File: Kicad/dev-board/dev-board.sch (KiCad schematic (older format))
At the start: 50 parts

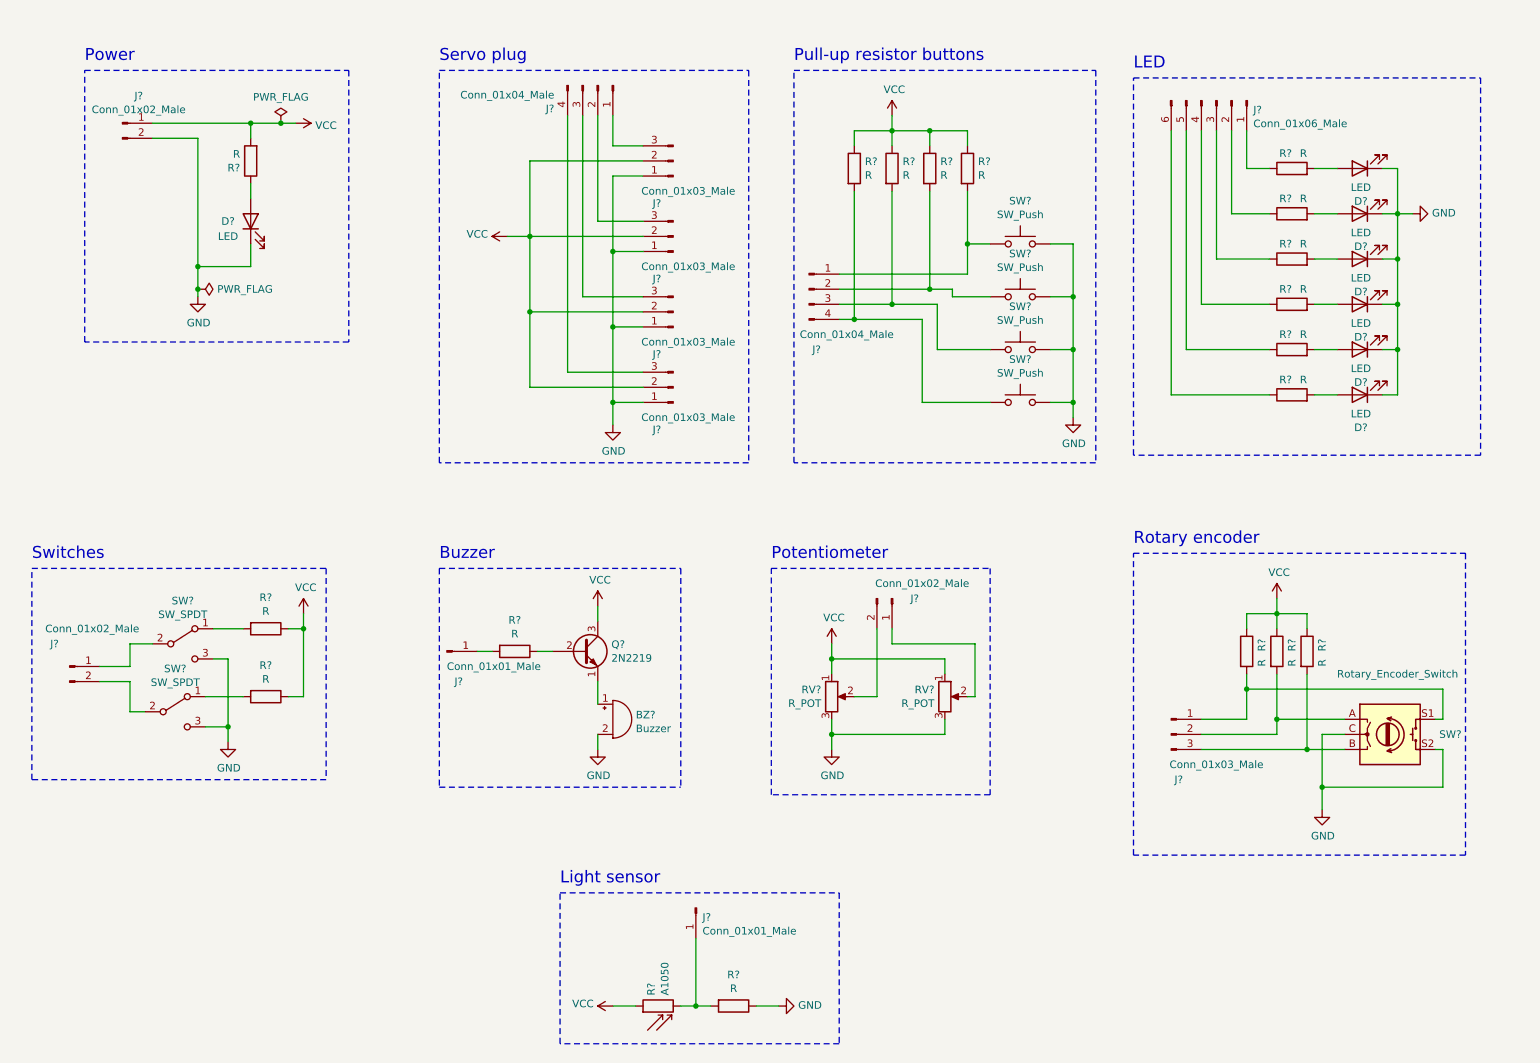
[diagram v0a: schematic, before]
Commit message: Add 555 timer + DIP switches
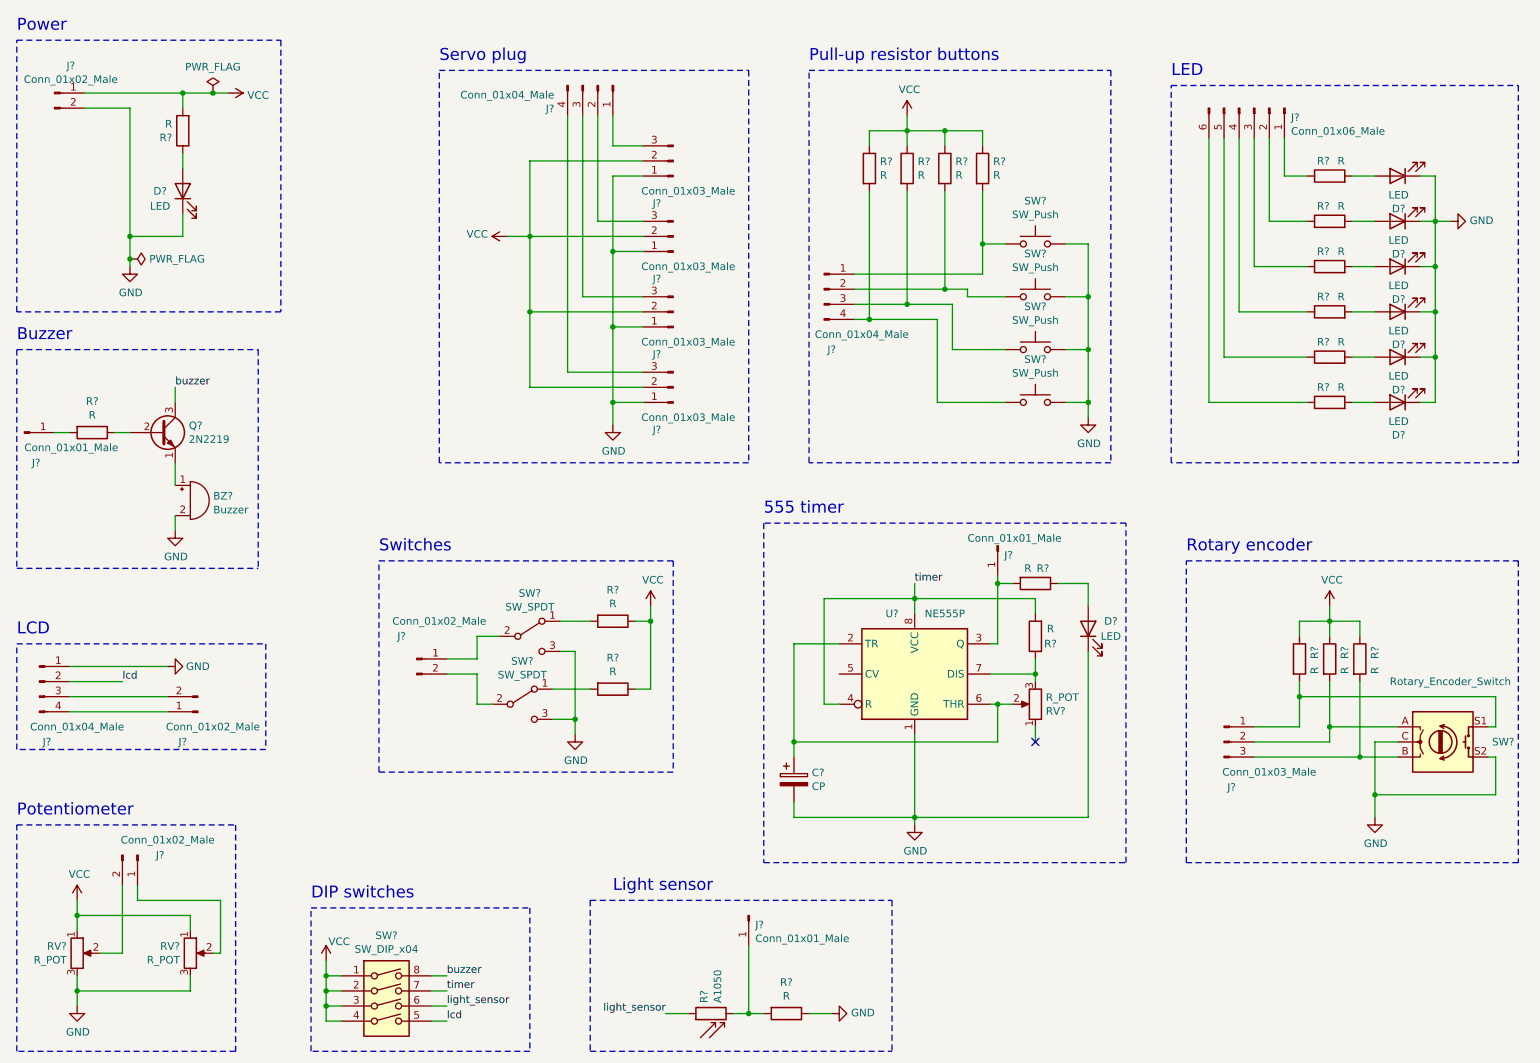
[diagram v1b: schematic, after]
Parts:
- added C?: CP, symbol Device:CP
- added D?: LED, symbol Device:LED
- added J?: Conn_01x01_Male, symbol Connector:Conn_01x01_Male
- added J?: Conn_01x04_Male, symbol Connector:Conn_01x04_Male
- added J?: Conn_01x02_Male, symbol Connector:Conn_01x02_Male
- added R? (x2): R, symbol Device:R
- added RV?: R_POT, symbol Device:R_POT
- added SW?: SW_DIP_x04, symbol Switch:SW_DIP_x04
- added U?: NE555P, Package_DIP:DIP-8_W7.62mm, symbol Timer:NE555P
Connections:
- net GND: now also C?.2, D?.1 (K), J?.1 (Pin_1), U?.1 (GND)
- net VCC: now also SW?.1, SW?.2, SW?.3, SW?.4; no longer Q?.3 (C), R?.1
- new net: C?.1, RV?.2, U?.2 (TR), U?.6 (THR)
- new net: J?.1 (Pin_1), R?.2, U?.3 (Q)
- new net: R?.1, RV?.3, U?.7 (DIS)
- new net: D?.2 (A), R?.1
- new net: J?.2 (Pin_2), J?.3 (Pin_3)
- new net: J?.1 (Pin_1), J?.4 (Pin_4)
- new net buzzer: Q?.3 (C), SW?.8
- new net lcd: J?.2 (Pin_2), SW?.5
- new net light_sensor: R?.1, SW?.6
- new net timer: R?.2, SW?.7, U?.4 (R), U?.8 (VCC)
- no-connect marks 0 -> 1
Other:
- note added: "555 timer"
- note added: "DIP switches"
- note added: "LCD"
- moved on the sheet: BZ?, D?, J?, Q?, R?, RV?, SW?

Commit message: Assign Footprint
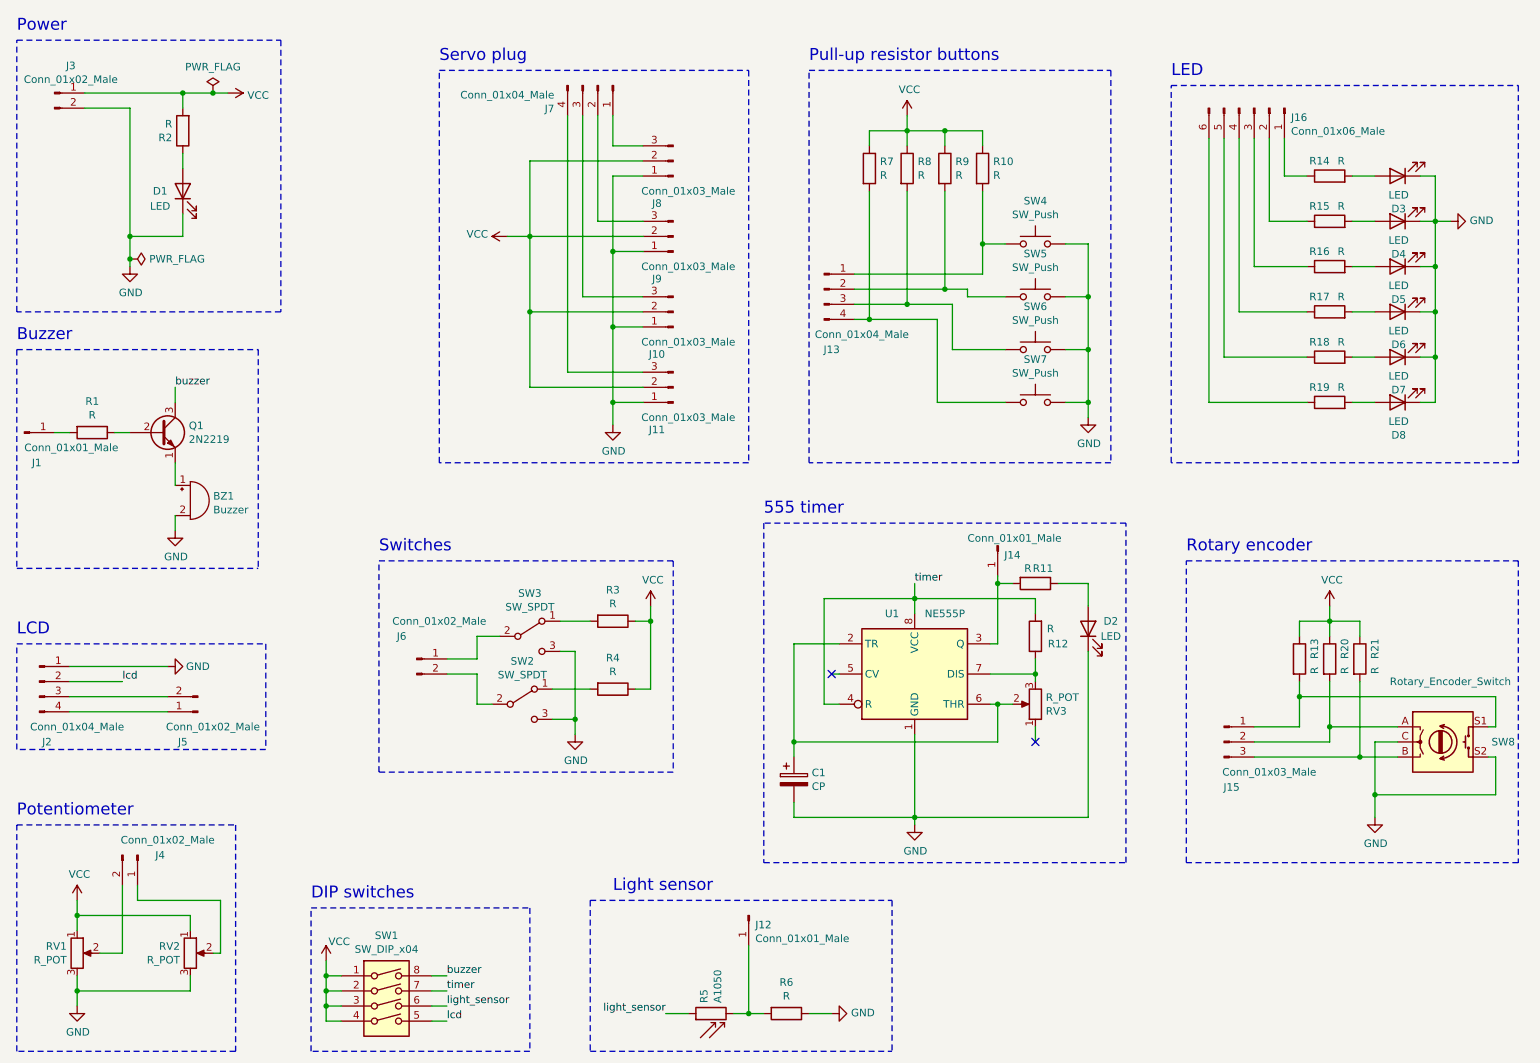
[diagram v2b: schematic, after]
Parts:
- BZ1: renamed from BZ?; footprint (none) -> Buzzer_Beeper:Buzzer_12x9.5RM7.6
- C1: renamed from C?; footprint (none) -> Capacitor_SMD:CP_Elec_5x5.3
- D1, D2, D3, D4, D5, D6, D7, D8: renamed from D?; footprint (none) -> LED_SMD:LED_0805_2012Metric_Pad1.15x1.40mm_HandSolder
- J1, J12, J14: renamed from J?; footprint (none) -> Connector_PinHeader_2.54mm:PinHeader_1x01_P2.54mm_Vertical
- J10, J11, J15, J8, J9: renamed from J?; footprint (none) -> Connector_PinHeader_2.54mm:PinHeader_1x03_P2.54mm_Vertical
- J13, J2, J7: renamed from J?; footprint (none) -> Connector_PinHeader_2.54mm:PinHeader_1x04_P2.54mm_Vertical
- J16: renamed from J?; footprint (none) -> Connector_PinHeader_2.54mm:PinHeader_1x06_P2.54mm_Vertical
- J3, J4, J5, J6: renamed from J?; footprint (none) -> Connector_PinHeader_2.54mm:PinHeader_1x02_P2.54mm_Vertical
- Q1: renamed from Q?; footprint Package_TO_SOT_THT:TO-39-3 -> Package_TO_SOT_SMD:SOT-23
- R1, R10, R11, R12, R13, R14, R15, R16, R17, R18, R19, R2, R20, R21, R3, R4, R6, R7, R8, R9: renamed from R?; footprint (none) -> Resistor_SMD:R_0815_2038Metric_Pad1.53x4.00mm_HandSolder
- R5: renamed from R?; footprint OptoDevice:R_LDR_D6.4mm_P3.4mm_Vertical -> OptoDevice:R_LDR_5.1x4.3mm_P3.4mm_Vertical
- RV3: renamed from RV?; footprint (none) -> Potentiometer_THT:Potentiometer_Piher_PT-6-V_Vertical
- SW1: renamed from SW?; footprint (none) -> Button_Switch_THT:SW_DIP_SPSTx04_Slide_9.78x12.34mm_W7.62mm_P2.54mm
- SW2, SW3: renamed from SW?; footprint (none) -> Connector_PinHeader_2.54mm:PinHeader_1x03_P2.54mm_Vertical
- SW4, SW5, SW6, SW7: renamed from SW?; footprint (none) -> Button_Switch_THT:SW_PUSH_6mm_H5mm
- SW8: renamed from SW?; footprint (none) -> Rotary_Encoder:RotaryEncoder_Alps_EC11E-Switch_Vertical_H20mm
- U1: renamed from U?; footprint Package_DIP:DIP-8_W7.62mm -> Package_DIP:DIP-8_W7.62mm_Socket
- gave numbers to parts that had none: 2
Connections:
- no-connect marks 1 -> 2
